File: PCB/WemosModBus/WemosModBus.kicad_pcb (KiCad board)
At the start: 2 copper layers, 38.1 x 66 mm, 14 parts, among them J1 Relay output, J2 Power, J3 Enable ModBus, J4 Software Seriel test #1, J5 Software Seriel test #2, M1 hw-726, U1 WeMos_mini, U2 MH-MINI-360

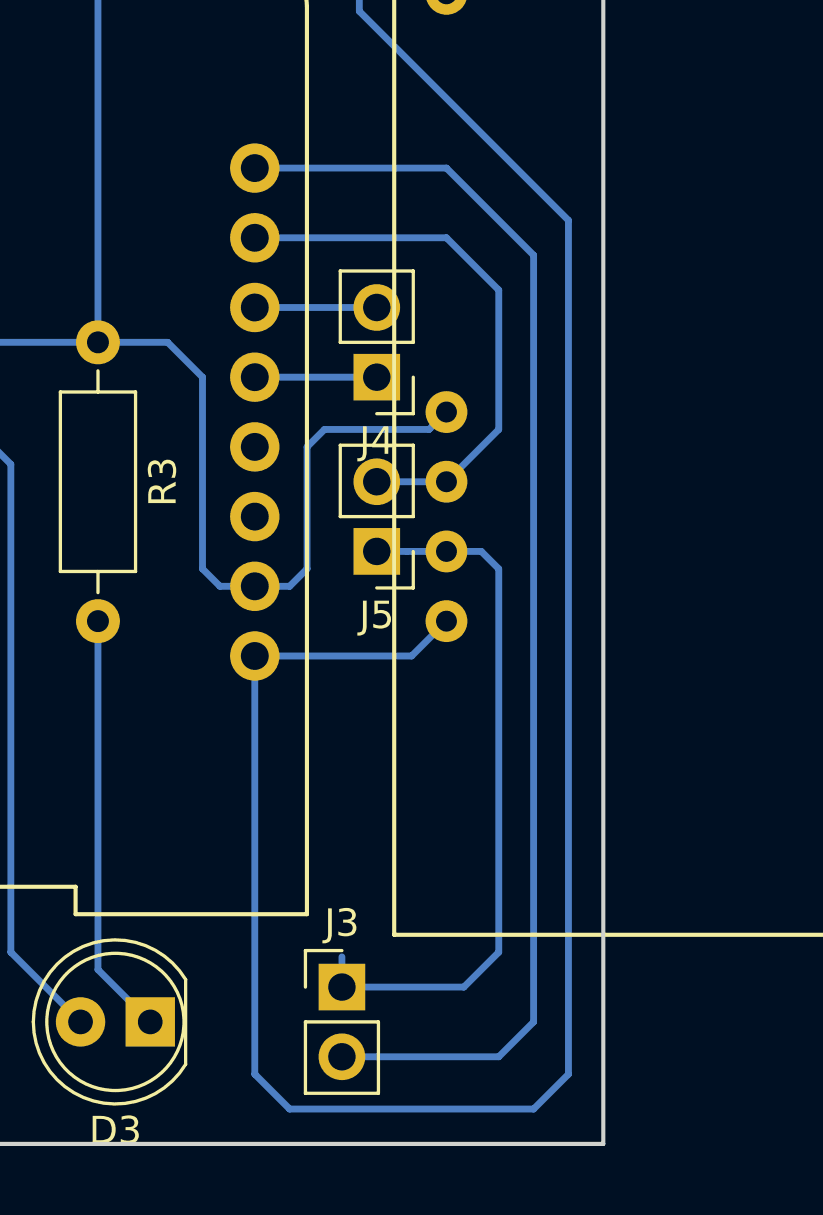
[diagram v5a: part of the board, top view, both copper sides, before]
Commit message: Using SoftwareSerial instead of RX/TX
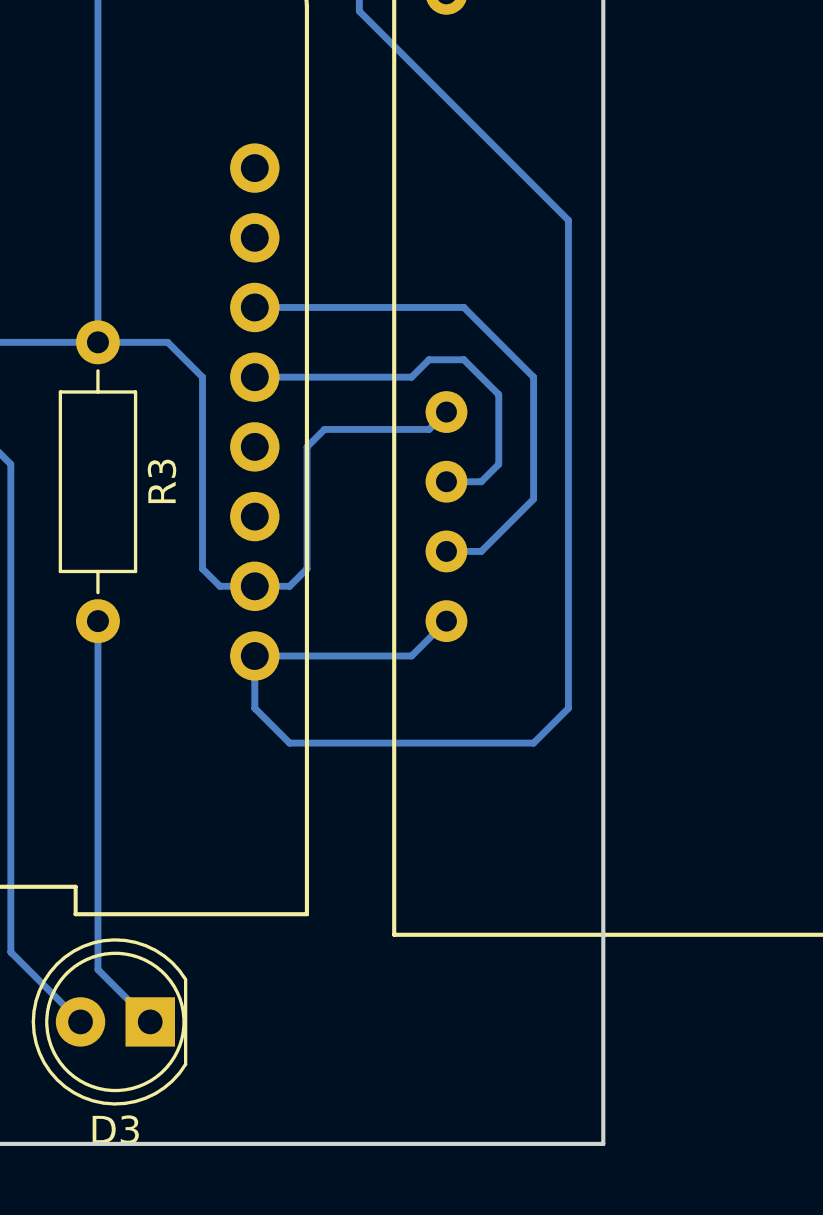
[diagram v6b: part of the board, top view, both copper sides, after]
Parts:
- removed J3: Enable ModBus, Connector_PinHeader_2.54mm:PinHeader_1x02_P2.54mm_Vertical
- removed J4: Software Seriel test #1, Connector_PinHeader_2.54mm:PinHeader_1x02_P2.54mm_Vertical
- removed J5: Software Seriel test #2, Connector_PinHeader_2.54mm:PinHeader_1x02_P2.54mm_Vertical
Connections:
- M1 pad 2: Net-(J3-Pad1) -> Net-(M1-Pad2)
- M1 pad 3: Net-(J5-Pad2) -> Net-(M1-Pad3)
- U1 pad 5: Net-(J4-Pad1) -> Net-(M1-Pad3)
- U1 pad 6: Net-(J4-Pad2) -> Net-(M1-Pad2)
- U1 pad 7: Net-(J5-Pad2) -> Net-(U1-Pad7)
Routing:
- net Net-(U1-Pad8): track 46.9 -> 0.00 mm
- net Net-(M1-Pad1): track 84.9 -> 58.2 mm
- net Net-(J3-Pad1): track 26.0 -> 0.00 mm
- net Net-(J5-Pad2): track 20.0 -> 0.00 mm
- net Net-(M1-Pad2): track 0.00 -> 19.6 mm
- net Net-(M1-Pad3): track 0.00 -> 14.4 mm
- net Net-(J4-Pad2): track 4.44 -> 0.00 mm
- net Net-(J4-Pad1): track 4.44 -> 0.00 mm
